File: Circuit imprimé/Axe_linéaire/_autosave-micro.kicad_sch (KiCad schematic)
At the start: 8 parts, among them Q1 LP2301LT1G, SW1 RESET, U1 PicoW

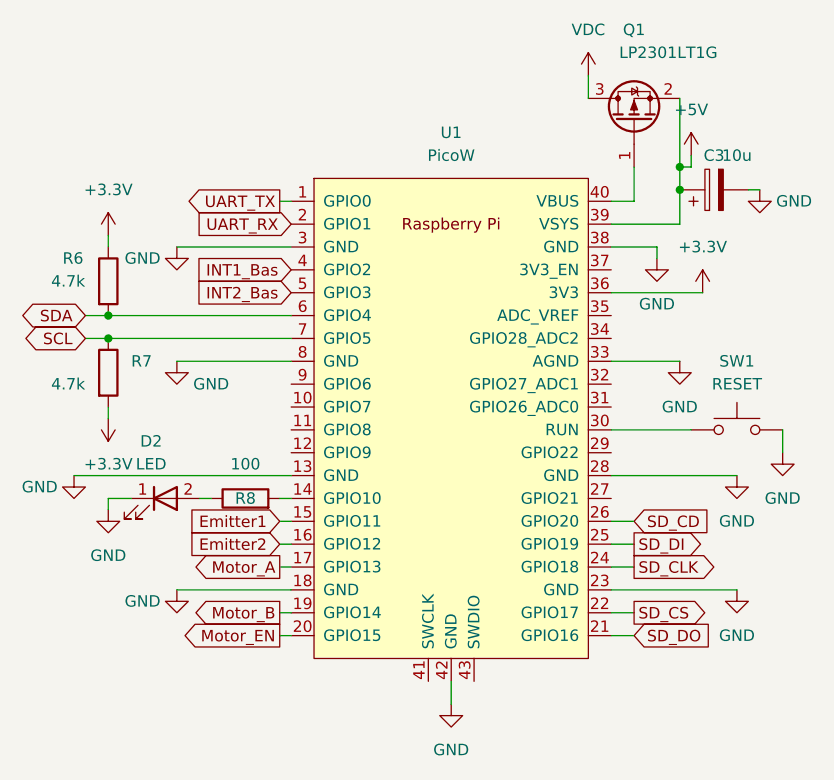
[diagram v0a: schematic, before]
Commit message: Création du circuit imprimé
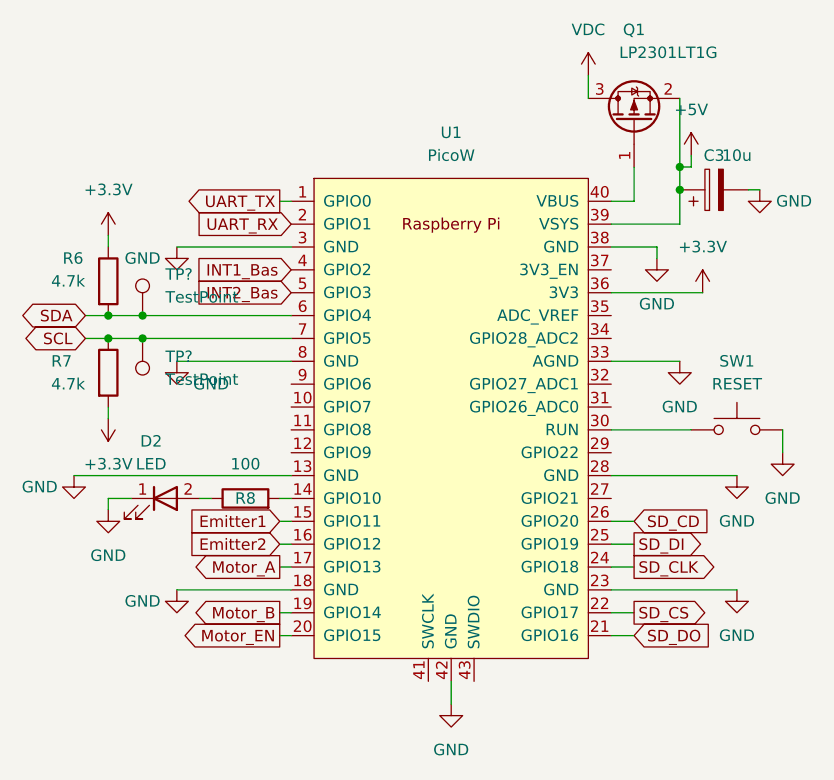
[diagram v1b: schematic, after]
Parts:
- added TP? (x2): TestPoint, symbol Connector:TestPoint
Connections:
- net SCL: now also TP?.1
- net SDA: now also TP?.1
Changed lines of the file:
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@@
   (junction (at 166.37 40.64) (diameter 0) (color 0 0 0 0)
   )
+  (junction (at 106.68 57.15) (diameter 0) (color 0 0 0 0)
+  )
   (junction (at 166.37 43.18) (diameter 0) (color 0 0 0 0)
   )
   (junction (at 102.87 59.69) (diameter 0) (color 0 0 0 0)
   )
+  (junction (at 106.68 59.69) (diameter 0) (color 0 0 0 0)
+  )
   (wire (pts (xy 158.75 85.09) (xy 161.29 85.09))
     (stroke (width 0) (type default) (color 0 0 0 0))
@@
     (stroke (width 0) (type default) (color 0 0 0 0))
   )
-  (wire (pts (xy 102.87 59.69) (xy 123.19 59.69))
+  (wire (pts (xy 102.87 59.69) (xy 106.68 59.69))
     (stroke (width 0) (type default) (color 0 0 0 0))
   )
@@
     (stroke (width 0) (type default) (color 0 0 0 0))
   )
+  (wire (pts (xy 106.68 59.69) (xy 123.19 59.69))
+    (stroke (width 0) (type default) (color 0 0 0 0))
+  )
   (wire (pts (xy 158.75 54.61) (xy 168.91 54.61))
     (stroke (width 0) (type default) (color 0 0 0 0))
@@
     (stroke (width 0) (type default) (color 0 0 0 0))
   )
-  (wire (pts (xy 102.87 57.15) (xy 123.19 57.15))
+  (wire (pts (xy 102.87 57.15) (xy 106.68 57.15))
     (stroke (width 0) (type default) (color 0 0 0 0))
   )
@@
   )
   (wire (pts (xy 158.75 49.53) (xy 163.83 49.53))
+    (stroke (width 0) (type default) (color 0 0 0 0))
+  )
+  (wire (pts (xy 106.68 57.15) (xy 123.19 57.15))
     (stroke (width 0) (type default) (color 0 0 0 0))
   )
@@
   (symbol (lib_id "Device:R") (at 102.87 63.5 0) (unit 1)
     (in_bom yes) (on_board yes)
-    (property "Reference" "R7" (id 0) (at 105.41 62.2299 0)
+    (property "Reference" "R7" (id 0) (at 96.52 62.23 0)
       (effects (font (size 1.27 1.27)) (justify left))
     )
@@
     (pin "1")
   )
+  (symbol (lib_id "Connector:TestPoint") (at 106.68 59.69 180) (unit 1)
+    (in_bom yes) (on_board yes) (fields_autoplaced)
+    (property "Reference" "TP?" (id 0) (at 109.22 61.7219 0)
+      (effects (font (size 1.27 1.27)) (justify right))
+    )
+    (property "Value" "TestPoint" (id 1) (at 109.22 64.2619 0)
+      (effects (font (size 1.27 1.27)) (justify right))
+    )
+    (property "Footprint" "" (id 2) (at 101.6 59.69 0)
+      (effects (font (size 1.27 1.27)) hide)
+    )
+    (property "Datasheet" "~" (id 3) (at 101.6 59.69 0)
+      (effects (font (size 1.27 1.27)) hide)
+    )
+    (pin "1")
+  )
   (symbol (lib_id "power:GND") (at 175.26 43.18 0) (unit 1)
     (in_bom yes) (on_board yes)
@@
       (effects (font (size 1.27 1.27)) hide)
     )
+    (pin "1")
+  )
+  (symbol (lib_id "Connector:TestPoint") (at 106.68 57.15 0) (unit 1)
+    (in_bom yes) (on_board yes) (fields_autoplaced)
+    (property "Reference" "TP?" (id 0) (at 109.22 52.5779 0)
+      (effects (font (size 1.27 1.27)) (justify left))
+    )
+    (property "Value" "TestPoint" (id 1) (at 109.22 55.1179 0)
+      (effects (font (size 1.27 1.27)) (justify left))
+    )
+    (property "Footprint" "" (id 2) (at 111.76 57.15 0)
+      (effects (font (size 1.27 1.27)) hide)
+    )
+    (property "Datasheet" "~" (id 3) (at 111.76 57.15 0)
+      (effects (font (size 1.27 1.27)) hide)
+    )
